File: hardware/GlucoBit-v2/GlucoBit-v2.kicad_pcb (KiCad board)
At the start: 4 copper layers, 55 x 30.4 mm, 43 parts, among them J1 USB-C-P16, J2 B2B-PH-K-S, J3 Conn_01x02_Socket, J6 B2B-PH-K-S, SW1 RESET, SW2 BOOT, U1 ESP32-S3-WROOM-1-N8, U2 BQ24040DSQR, U3 TLV75801PDBV, U4 USBLC6-2SC6, U5 MAX98357AETE+T, U6 08JQ-BT

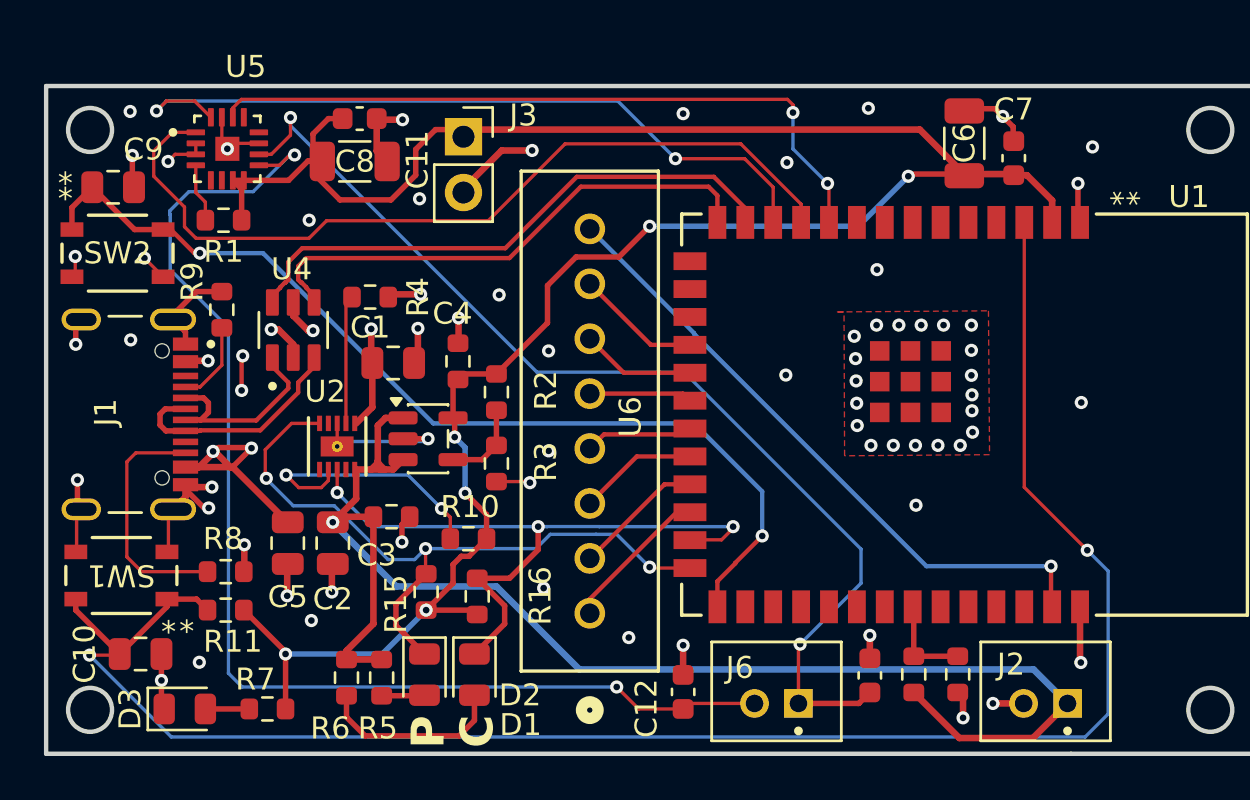
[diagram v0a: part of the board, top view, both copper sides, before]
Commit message: Ran initial DFM, Updated routing + gerbers
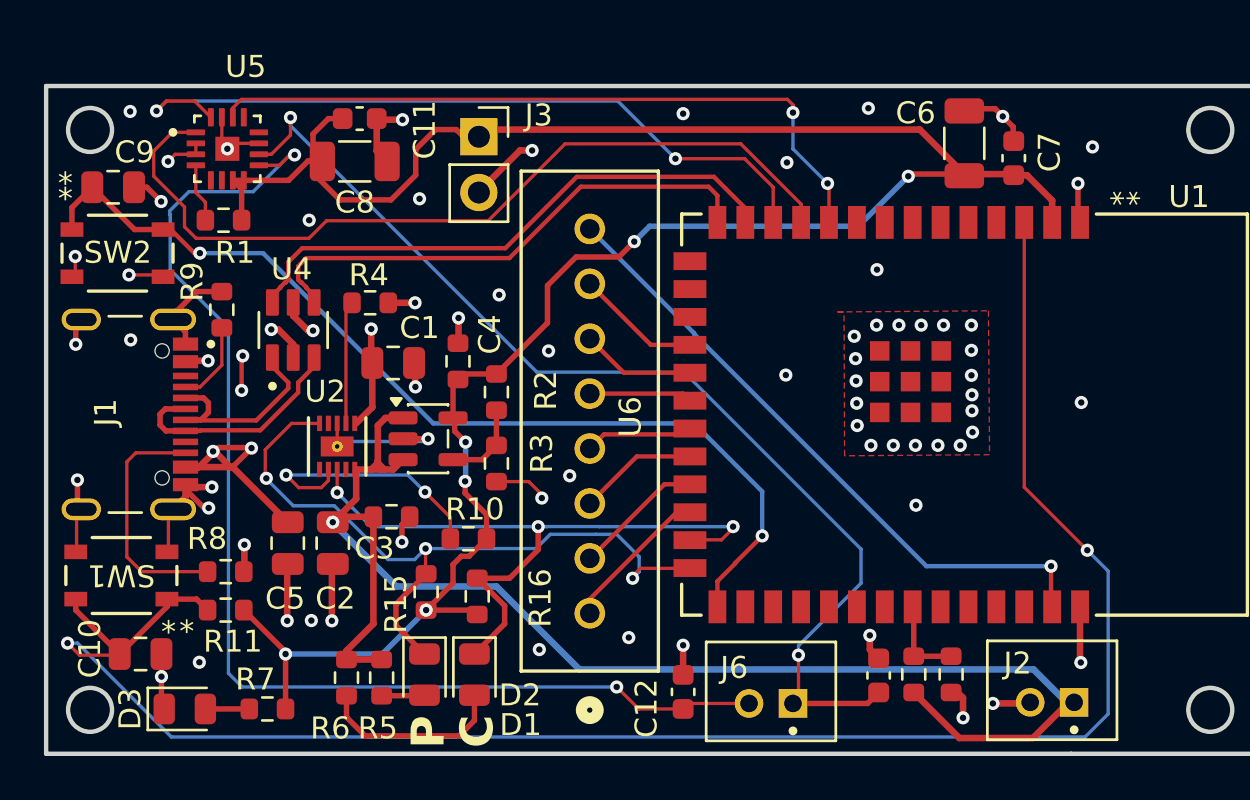
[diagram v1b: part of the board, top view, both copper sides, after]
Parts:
- moved J3 0.70 mm to (80.7, 40.7)
- moved C13 0.40 mm to (98.9, 65.2)
- moved J2 0.30 mm to (106.8, 65.9)
- moved R14 0.30 mm to (102.2, 65.2)
- moved R4 0.26 mm to (75.8, 48.3)
- moved J6 0.25 mm to (94.0, 66.0)
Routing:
- net GND: track 66.5 -> 69.5 mm
- net ENABLE: track 82.5 -> 84.9 mm
- net PGOOD: track 32.4 -> 33.8 mm
- net Net-(U5-OUTN): track 48.6 -> 49.4 mm
- net /VOUT: track 65.4 -> 66.1 mm

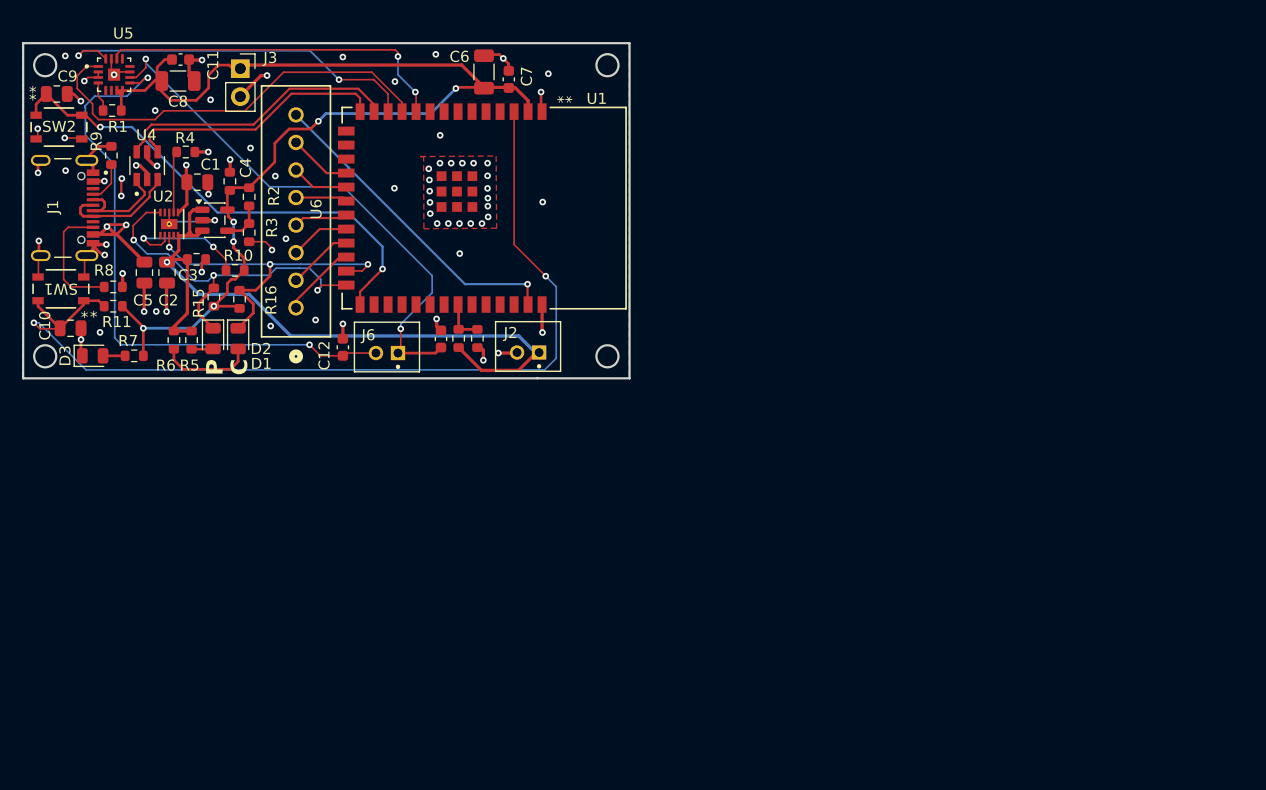
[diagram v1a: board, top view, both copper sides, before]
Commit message: Ran #2 DFM, Updated routing + gerbers
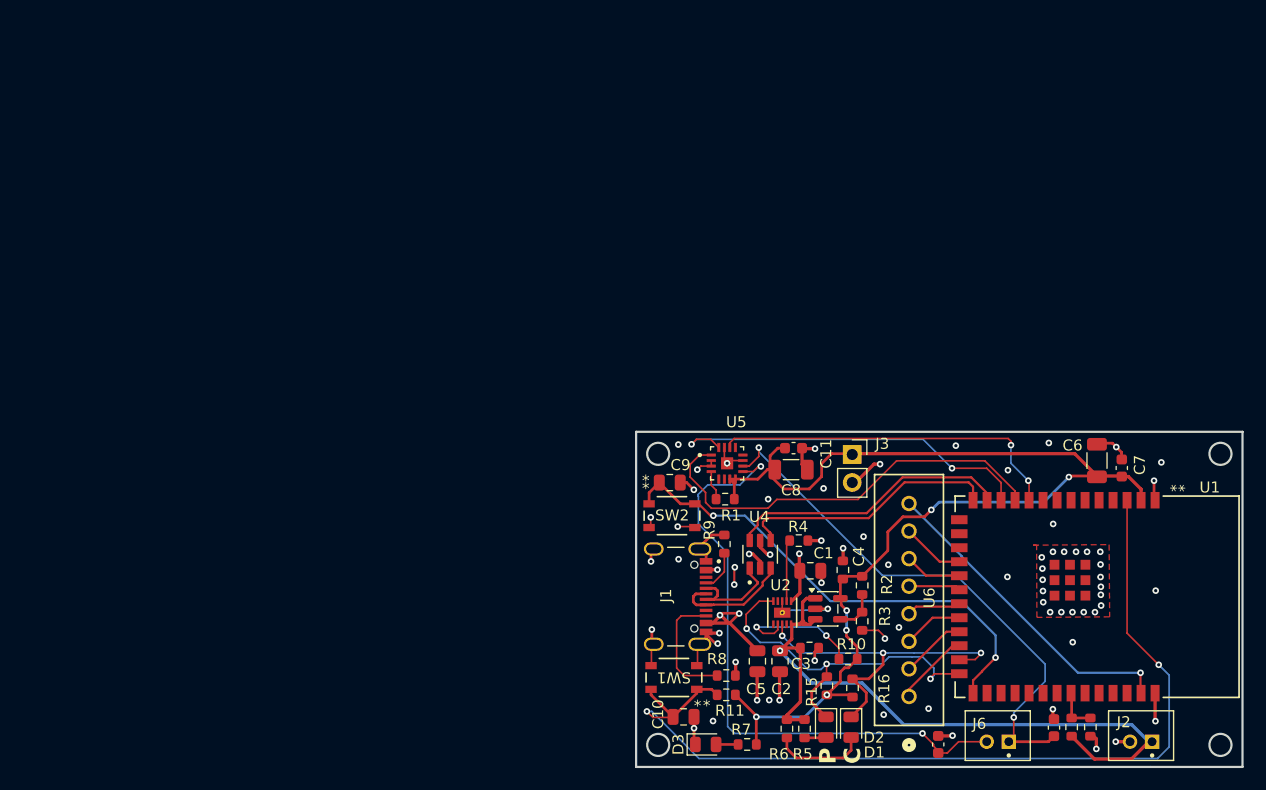
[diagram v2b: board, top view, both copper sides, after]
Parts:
- moved J2 65.9 mm to (162.4, 101.2)
- moved C1 65.8 mm to (132.4, 86.2)
- moved C10 65.8 mm to (120.9, 99.5)
- moved C13 65.8 mm to (154.5, 100.5)
- moved C2 65.8 mm to (129.7, 94.4)
- moved C6 65.8 mm to (158.4, 76.2)
- moved C7 65.8 mm to (160.7, 76.9)
- moved C8 65.8 mm to (130.7, 77.1)
- moved C9 65.8 mm to (119.7, 78.2)
- moved R11 65.8 mm to (124.8, 97.5)
- moved R14 65.8 mm to (157.8, 100.4)
- moved R15 65.8 mm to (133.9, 96.7)
- moved R4 65.8 mm to (131.3, 83.5)
- moved R6 65.8 mm to (130.3, 100.6)
- moved R8 65.8 mm to (124.8, 95.7)
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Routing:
- net GND: track 69.5 -> 68.7 mm
- net Net-(U5-OUTP): track 55.2 -> 55.8 mm

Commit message: Update UI
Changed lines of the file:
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@@
 		(tags "capacitor")
 		(property "Reference" "C12"
-			(at 0 0 -270)
+			(at 0 0 90)
 			(layer "B.SilkS")
 			(effects
@@
 	)
 	(via
-		(at 128.575 79.748836)
+		(at 128 79.1)
 		(size 0.6)
 		(drill 0.29)
@@
 	)
 	(segment
-		(start 140.225 76.273836)
-		(end 136.725 79.773836)
+		(start 121.5 76.598836)
+		(end 122.35 75.748836)
 		(width 0.1524)
 		(layer "F.Cu")
@@
 	)
 	(segment
-		(start 121.5 76.598836)
-		(end 122.35 75.748836)
+		(start 121.5 77.748836)
+		(end 121.5 76.598836)
 		(width 0.1524)
 		(layer "F.Cu")
@@
 	)
 	(segment
-		(start 121.5 77.748836)
-		(end 121.5 76.598836)
+		(start 122.9 79.148836)
+		(end 121.5 77.748836)
 		(width 0.1524)
 		(layer "F.Cu")
@@
 	)
 	(segment
-		(start 123.425 80.573836)
-		(end 122.9 80.048836)
+		(start 150.97 79.019053)
+		(end 148.224783 76.273836)
 		(width 0.1524)
 		(layer "F.Cu")
@@
 	)
 	(segment
-		(start 150.97 79.848836)
-		(end 150.97 79.019053)
+		(start 128.026164 79.773836)
+		(end 127.226164 80.573836)
 		(width 0.1524)
 		(layer "F.Cu")
@@
 	)
 	(segment
-		(start 150.97 79.019053)
-		(end 148.224783 76.273836)
+		(start 123.425 80.573836)
+		(end 122.9 80.048836)
 		(width 0.1524)
 		(layer "F.Cu")
@@
 	)
 	(segment
-		(start 122.9 79.148836)
-		(end 121.5 77.748836)
+		(start 150.97 79.848836)
+		(end 150.97 79.019053)
 		(width 0.1524)
 		(layer "F.Cu")
@@
 	)
 	(segment
-		(start 128.566285 80.573836)
-		(end 123.425 80.573836)
+		(start 136.725 79.773836)
+		(end 128.026164 79.773836)
 		(width 0.1524)
 		(layer "F.Cu")
@@
 	)
 	(segment
-		(start 129.366285 79.773836)
-		(end 128.566285 80.573836)
+		(start 127.226164 80.573836)
+		(end 123.425 80.573836)
 		(width 0.1524)
 		(layer "F.Cu")
@@
 	)
 	(segment
-		(start 136.725 79.773836)
-		(end 129.366285 79.773836)
+		(start 140.225 76.273836)
+		(end 136.725 79.773836)
 		(width 0.1524)
 		(layer "F.Cu")

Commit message: Generated STEP files
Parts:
- moved C11 0.57 mm to (130.3, 75.1)
- moved C8 0.35 mm to (130.3, 77.1)
- moved J6 0.11 mm to (149.3, 101.2)
- moved C12 0.10 mm to (143.9, 102.0)
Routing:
- net +3V3: track 105.3 -> 103.8 mm
- net GND: track 68.7 -> 69.5 mm
- net Net-(U5-OUTP): track 55.8 -> 55.2 mm
